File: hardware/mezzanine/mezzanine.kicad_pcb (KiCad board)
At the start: 4 copper layers, 85 x 56 mm, 34 parts, among them J1 USB_A, J2 USB_C, J3 HDMI_D, J4 HDMI_D, U1 AP22653W6, U2 TPD4EUSB30, U3 TPD4EUSB30, U4 TPD4EUSB30, U5 MagJack-A70-112-331N126, U6 RT9742SNGV, U7 74LVC1G07SE-7

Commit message: cam v2
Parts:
- C2: footprint Capacitor_Tantalum_SMD:CP_EIA-2012-12_Kemet-R -> Capacitor_Tantalum_SMD:CP_EIA-7343-31_Kemet-D
- C7, C8, C9: value 0.1 uF -> 100n
- R1: value 14k -> 15K 1%
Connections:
- J3 pad 2: (no net) -> unconnected-(J3-Pad2)
- J4 pad 2: (no net) -> unconnected-(J4-Pad2)
- Module1 pad 49: (no net) -> /AnalogIP1
- Module1 pad 51: (no net) -> /AnalogIP0
- Module2 pad 1: (no net) -> unconnected-(Module2-Pad1)
- Module2 pad 10: (no net) -> unconnected-(Module2-Pad10)
- Module2 pad 100: (no net) -> unconnected-(Module2-Pad100)
- Module2 pad 11: (no net) -> unconnected-(Module2-Pad11)
- Module2 pad 12: (no net) -> unconnected-(Module2-Pad12)
- Module2 pad 13: (no net) -> unconnected-(Module2-Pad13)
- Module2 pad 14: (no net) -> unconnected-(Module2-Pad14)
- Module2 pad 15: (no net) -> unconnected-(Module2-Pad15)
- Module2 pad 16: (no net) -> unconnected-(Module2-Pad16)
- Module2 pad 17: (no net) -> unconnected-(Module2-Pad17)
- Module2 pad 18: (no net) -> unconnected-(Module2-Pad18)
- Module2 pad 19: (no net) -> unconnected-(Module2-Pad19)
- Module2 pad 2: (no net) -> unconnected-(Module2-Pad2)
- Module2 pad 20: (no net) -> unconnected-(Module2-Pad20)
- Module2 pad 21: (no net) -> unconnected-(Module2-Pad21)
- Module2 pad 22: (no net) -> unconnected-(Module2-Pad22)
- Module2 pad 23: (no net) -> unconnected-(Module2-Pad23)
- Module2 pad 24: (no net) -> unconnected-(Module2-Pad24)
- Module2 pad 25: (no net) -> unconnected-(Module2-Pad25)
- Module2 pad 26: (no net) -> unconnected-(Module2-Pad26)
- Module2 pad 27: (no net) -> unconnected-(Module2-Pad27)
- Module2 pad 28: (no net) -> unconnected-(Module2-Pad28)
- Module2 pad 29: (no net) -> unconnected-(Module2-Pad29)
- Module2 pad 3: (no net) -> unconnected-(Module2-Pad3)
- Module2 pad 30: (no net) -> unconnected-(Module2-Pad30)
- Module2 pad 31: (no net) -> unconnected-(Module2-Pad31)
- Module2 pad 32: (no net) -> unconnected-(Module2-Pad32)
- Module2 pad 33: (no net) -> unconnected-(Module2-Pad33)
- Module2 pad 34: (no net) -> unconnected-(Module2-Pad34)
- Module2 pad 35: (no net) -> unconnected-(Module2-Pad35)
- Module2 pad 36: (no net) -> unconnected-(Module2-Pad36)
- Module2 pad 37: (no net) -> unconnected-(Module2-Pad37)
- Module2 pad 38: (no net) -> unconnected-(Module2-Pad38)
- Module2 pad 39: (no net) -> unconnected-(Module2-Pad39)
- Module2 pad 4: (no net) -> unconnected-(Module2-Pad4)
- Module2 pad 40: (no net) -> unconnected-(Module2-Pad40)
- Module2 pad 41: (no net) -> unconnected-(Module2-Pad41)
- Module2 pad 42: (no net) -> unconnected-(Module2-Pad42)
- Module2 pad 43: (no net) -> unconnected-(Module2-Pad43)
- Module2 pad 44: (no net) -> unconnected-(Module2-Pad44)
- Module2 pad 45: (no net) -> unconnected-(Module2-Pad45)
- Module2 pad 46: (no net) -> unconnected-(Module2-Pad46)
- Module2 pad 47: (no net) -> unconnected-(Module2-Pad47)
- Module2 pad 48: (no net) -> unconnected-(Module2-Pad48)
- Module2 pad 49: (no net) -> unconnected-(Module2-Pad49)
- Module2 pad 5: (no net) -> unconnected-(Module2-Pad5)
- Module2 pad 50: (no net) -> unconnected-(Module2-Pad50)
- Module2 pad 51: (no net) -> unconnected-(Module2-Pad51)
- Module2 pad 52: (no net) -> unconnected-(Module2-Pad52)
- Module2 pad 53: (no net) -> unconnected-(Module2-Pad53)
- Module2 pad 54: (no net) -> unconnected-(Module2-Pad54)
- Module2 pad 55: (no net) -> unconnected-(Module2-Pad55)
- Module2 pad 56: (no net) -> unconnected-(Module2-Pad56)
- Module2 pad 57: (no net) -> unconnected-(Module2-Pad57)
- Module2 pad 58: (no net) -> unconnected-(Module2-Pad58)
- Module2 pad 59: (no net) -> unconnected-(Module2-Pad59)
- Module2 pad 6: (no net) -> unconnected-(Module2-Pad6)
- Module2 pad 60: (no net) -> unconnected-(Module2-Pad60)
- Module2 pad 61: (no net) -> unconnected-(Module2-Pad61)
- Module2 pad 62: (no net) -> unconnected-(Module2-Pad62)
- Module2 pad 63: (no net) -> unconnected-(Module2-Pad63)
- Module2 pad 64: (no net) -> unconnected-(Module2-Pad64)
- Module2 pad 65: (no net) -> unconnected-(Module2-Pad65)
- Module2 pad 66: (no net) -> unconnected-(Module2-Pad66)
- Module2 pad 67: (no net) -> unconnected-(Module2-Pad67)
- Module2 pad 68: (no net) -> unconnected-(Module2-Pad68)
- Module2 pad 69: (no net) -> unconnected-(Module2-Pad69)
- Module2 pad 7: (no net) -> unconnected-(Module2-Pad7)
- Module2 pad 70: (no net) -> unconnected-(Module2-Pad70)
- Module2 pad 71: (no net) -> unconnected-(Module2-Pad71)
- Module2 pad 72: (no net) -> unconnected-(Module2-Pad72)
- Module2 pad 73: (no net) -> unconnected-(Module2-Pad73)
- Module2 pad 74: (no net) -> unconnected-(Module2-Pad74)
- Module2 pad 75: (no net) -> unconnected-(Module2-Pad75)
- Module2 pad 76: (no net) -> unconnected-(Module2-Pad76)
- Module2 pad 77: (no net) -> unconnected-(Module2-Pad77)
- Module2 pad 78: (no net) -> unconnected-(Module2-Pad78)
- Module2 pad 79: (no net) -> unconnected-(Module2-Pad79)
- Module2 pad 8: (no net) -> unconnected-(Module2-Pad8)
- Module2 pad 80: (no net) -> unconnected-(Module2-Pad80)
- Module2 pad 81: (no net) -> unconnected-(Module2-Pad81)
- Module2 pad 82: (no net) -> unconnected-(Module2-Pad82)
- Module2 pad 83: (no net) -> unconnected-(Module2-Pad83)
- Module2 pad 84: (no net) -> unconnected-(Module2-Pad84)
- Module2 pad 85: (no net) -> unconnected-(Module2-Pad85)
- Module2 pad 86: (no net) -> unconnected-(Module2-Pad86)
- Module2 pad 87: (no net) -> unconnected-(Module2-Pad87)
- Module2 pad 88: (no net) -> unconnected-(Module2-Pad88)
- Module2 pad 89: (no net) -> unconnected-(Module2-Pad89)
- Module2 pad 9: (no net) -> unconnected-(Module2-Pad9)
- Module2 pad 90: (no net) -> unconnected-(Module2-Pad90)
- Module2 pad 91: (no net) -> unconnected-(Module2-Pad91)
- Module2 pad 92: (no net) -> unconnected-(Module2-Pad92)
- Module2 pad 93: (no net) -> unconnected-(Module2-Pad93)
- Module2 pad 94: (no net) -> unconnected-(Module2-Pad94)
- Module2 pad 95: (no net) -> unconnected-(Module2-Pad95)
- Module2 pad 96: (no net) -> unconnected-(Module2-Pad96)
- Module2 pad 97: (no net) -> unconnected-(Module2-Pad97)
- Module2 pad 98: (no net) -> unconnected-(Module2-Pad98)
- Module2 pad 99: (no net) -> unconnected-(Module2-Pad99)
- U1 pad 4: (no net) -> /usb/nUSB_CURR_FAULT
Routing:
- net GND: track 22.9 -> 25.6 mm, vias 49 -> 58
- net /HDMI1_HOTPLUG: track 34.1 -> 36.8 mm
- net /usb/USB2_HOST_VBUS: track 25.0 -> 22.4 mm
- net /HDMI0_CEC: track 65.4 -> 63.8 mm
- net /HDMI0_HOTPLUG: track 44.6 -> 45.8 mm
- net /HDMI1_TX0_N: track 45.1 -> 44.2 mm, vias 1 -> 2
- net Net-(J2-PadA5): track 16.1 -> 15.3 mm
- net /USB2_DEV_P: track 80.0 -> 80.9 mm
- net /HDMI1_CEC: track 47.8 -> 48.5 mm
- net /USB2_DEV_N: track 82.7 -> 83.3 mm
- net /HDMI1_SDA: track 34.8 -> 35.4 mm
- net /HDMI1_TX0_P: track 44.9 -> 45.0 mm, vias 1 -> 2

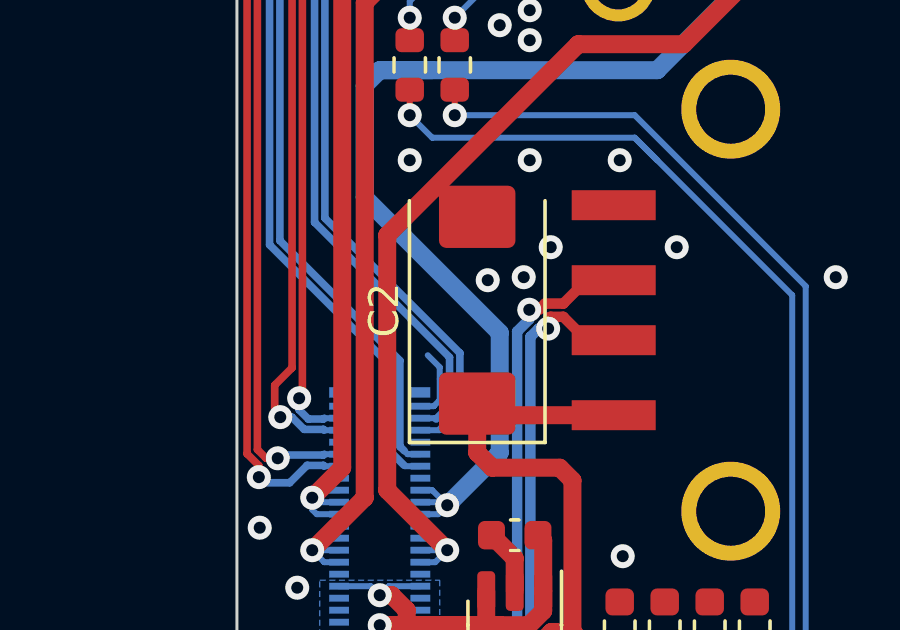
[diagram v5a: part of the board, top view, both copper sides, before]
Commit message: update USB-A host capacitor footprint
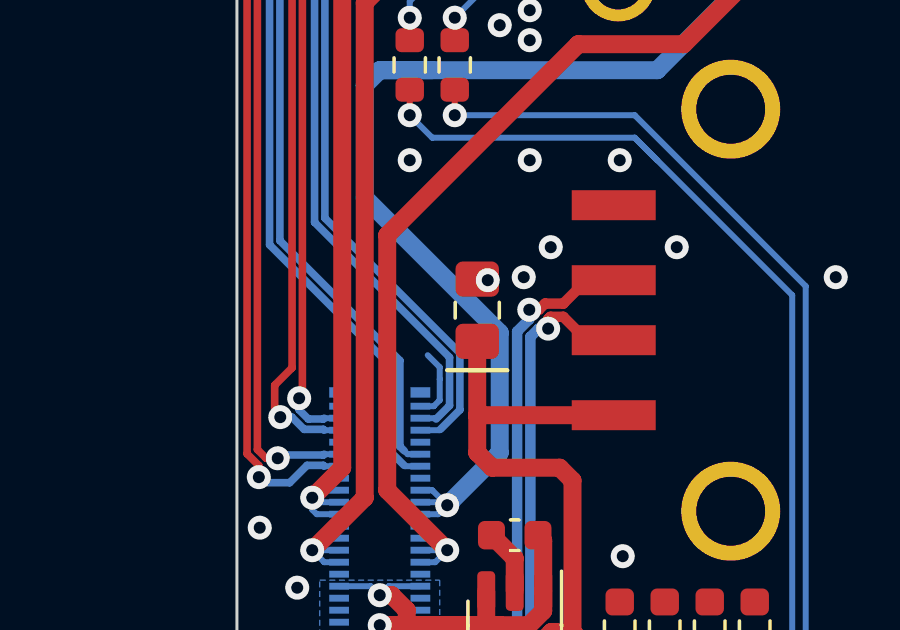
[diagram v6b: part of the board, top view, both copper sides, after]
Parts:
- C2: footprint Capacitor_Tantalum_SMD:CP_EIA-7343-31_Kemet-D -> Capacitor_SMD:C_0805_2012Metric_Pad1.18x1.45mm_HandSolder
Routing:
- net /usb/USB2_HOST_VBUS: track 22.4 -> 24.9 mm
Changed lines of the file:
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@@
     )
   )
-  (footprint "Capacitor_Tantalum_SMD:CP_EIA-7343-31_Kemet-D" (layer "F.Cu")
+  (footprint "Capacitor_SMD:C_0805_2012Metric_Pad1.18x1.45mm_HandSolder" (layer "F.Cu")
     (at 89.25 49 90)
-    (descr "Tantalum Capacitor SMD Kemet-D (7343-31 Metric), IPC_7351 nominal, (Body size from: http://www.kemet.com/Lists/ProductCatalog/Attachments/253/KEM_TC101_STD.pdf), generated with kicad-footprint-generator")
-    (tags "capacitor tantalum")
+    (descr "Capacitor SMD 0805 (2012 Metric), square (rectangular) end terminal, IPC_7351 nominal with elongated pad for handsoldering. (Body size source: IPC-SM-782 page 76, https://www.pcb-3d.com/wordpress/wp-content/uploads/ipc-sm-782a_amendment_1_and_2.pdf, https://docs.google.com/spreadsheets/d/1BsfQQcO9C6DZCsRaXUlFlo91Tg2WpOkGARC1WS5S8t0/edit?usp=sharing), generated with kicad-footprint-generator")
+    (tags "capacitor handsolder")
     (property "Field4" "Mouser")
     (property "Field5" "667-EEF-CX0J101R")
@@
     (property "Sheetname" "usb")
     (attr smd)
-    (fp_text reference "C2" (at 0 -3.1 90) (layer "F.SilkS")
+    (fp_text reference "C2" (at 0 -1.68 90) (layer "F.SilkS") hide
       (effects (font (size 1 1) (thickness 0.15)))
     )
-    (fp_text value "100uF" (at 0 3.1 90) (layer "F.Fab")
+    (fp_text value "100uF" (at 0 1.68 90) (layer "F.Fab") hide
       (effects (font (size 1 1) (thickness 0.15)))
     )
-    (fp_text user "${REFERENCE}" (at 0 0 90) (layer "F.Fab")
-      (effects (font (size 1 1) (thickness 0.15)))
+    (fp_text user "${REFERENCE}" (at 0 0 90) (layer "F.Fab") hide
+      (effects (font (size 0.5 0.5) (thickness 0.08)))
     )
-    (fp_line (start -4.41 2.26) (end 3.65 2.26) (layer "F.SilkS") (width 0.12))
-    (fp_line (start -4.41 -2.26) (end -4.41 2.26) (layer "F.SilkS") (width 0.12))
-    (fp_line (start 3.65 -2.26) (end -4.41 -2.26) (layer "F.SilkS") (width 0.12))
-    (fp_line (start -4.4 -2.4) (end 4.4 -2.4) (layer "F.CrtYd") (width 0.05))
-    (fp_line (start 4.4 -2.4) (end 4.4 2.4) (layer "F.CrtYd") (width 0.05))
-    (fp_line (start -4.4 2.4) (end -4.4 -2.4) (layer "F.CrtYd") (width 0.05))
-    (fp_line (start 4.4 2.4) (end -4.4 2.4) (layer "F.CrtYd") (width 0.05))
-    (fp_line (start 3.65 2.15) (end 3.65 -2.15) (layer "F.Fab") (width 0.1))
-    (fp_line (start -3.65 -1.15) (end -3.65 2.15) (layer "F.Fab") (width 0.1))
-    (fp_line (start 3.65 -2.15) (end -2.65 -2.15) (layer "F.Fab") (width 0.1))
-    (fp_line (start -3.65 2.15) (end 3.65 2.15) (layer "F.Fab") (width 0.1))
-    (fp_line (start -2.65 -2.15) (end -3.65 -1.15) (layer "F.Fab") (width 0.1))
-    (pad "1" smd roundrect locked (at -3.1125 0 90) (size 2.075 2.55) (layers "F.Cu" "F.Paste" "F.Mask") (roundrect_rratio 0.1204819277)
+    (fp_line (start -0.261252 -0.735) (end 0.261252 -0.735) (layer "F.SilkS") (width 0.12))
+    (fp_line (start -0.261252 0.735) (end 0.261252 0.735) (layer "F.SilkS") (width 0.12))
+    (fp_line (start 1.88 0.98) (end -1.88 0.98) (layer "F.CrtYd") (width 0.05))
+    (fp_line (start -1.88 0.98) (end -1.88 -0.98) (layer "F.CrtYd") (width 0.05))
+    (fp_line (start -1.88 -0.98) (end 1.88 -0.98) (layer "F.CrtYd") (width 0.05))
+    (fp_line (start 1.88 -0.98) (end 1.88 0.98) (layer "F.CrtYd") (width 0.05))
+    (fp_line (start 1 0.625) (end -1 0.625) (layer "F.Fab") (width 0.1))
+    (fp_line (start -1 0.625) (end -1 -0.625) (layer "F.Fab") (width 0.1))
+    (fp_line (start 1 -0.625) (end 1 0.625) (layer "F.Fab") (width 0.1))
+    (fp_line (start -1 -0.625) (end 1 -0.625) (layer "F.Fab") (width 0.1))
+    (pad "1" smd roundrect locked (at -1.0375 0 90) (size 1.175 1.45) (layers "F.Cu" "F.Paste" "F.Mask") (roundrect_rratio 0.212766)
       (net 2 "/usb/USB2_HOST_VBUS") (pintype "passive"))
-    (pad "2" smd roundrect locked (at 3.1125 0 90) (size 2.075 2.55) (layers "F.Cu" "F.Paste" "F.Mask") (roundrect_rratio 0.1204819277)
+    (pad "2" smd roundrect locked (at 1.0375 0 90) (size 1.175 1.45) (layers "F.Cu" "F.Paste" "F.Mask") (roundrect_rratio 0.212766)
       (net 1 "GND") (pintype "passive"))
-    (model "${KICAD6_3DMODEL_DIR}/Capacitor_Tantalum_SMD.3dshapes/CP_EIA-7343-31_Kemet-D.wrl"
+    (model "${KICAD6_3DMODEL_DIR}/Capacitor_SMD.3dshapes/C_0805_2012Metric.wrl"
       (offset (xyz 0 0 0))
       (scale (xyz 1 1 1))
@@
     )
   )
+  (gr_line (start 88.25 51) (end 90.25 51) (layer "F.SilkS") (width 0.15))
   (gr_arc (start 102 73) (end 102 76) (angle -90) (layer "Edge.Cuts") (width 0.1))
   (gr_line (start 81.24 28.53) (end 81.24 62.53) (layer "Edge.Cuts") (width 0.1))
@@
   (segment (start 92 54.25) (end 89.75 54.25) (width 0.6) (layer "F.Cu") (net 2))
   (segment (start 91.45 60.6375) (end 91.45 60.000128) (width 0.6) (layer "F.Cu") (net 2))
+  (segment (start 89.25 52.5) (end 89.25 50.0375) (width 0.6) (layer "F.Cu") (net 2))
   (segment (start 92.975 60.275) (end 94 60.275) (width 0.6) (layer "F.Cu") (net 2))
   (segment (start 93.8 52.5) (end 89.25 52.5) (width 0.6) (layer "F.Cu") (net 2))
